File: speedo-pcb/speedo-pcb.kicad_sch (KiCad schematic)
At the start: 54 parts, among them J1 Debug, J2 Mode, J3 Speedo, J4 Power, J5 VBAT, J6 BOOT, J7 Breakout, M1 X27_128, U1 XC6206P332MR, U3 OLED_128x32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

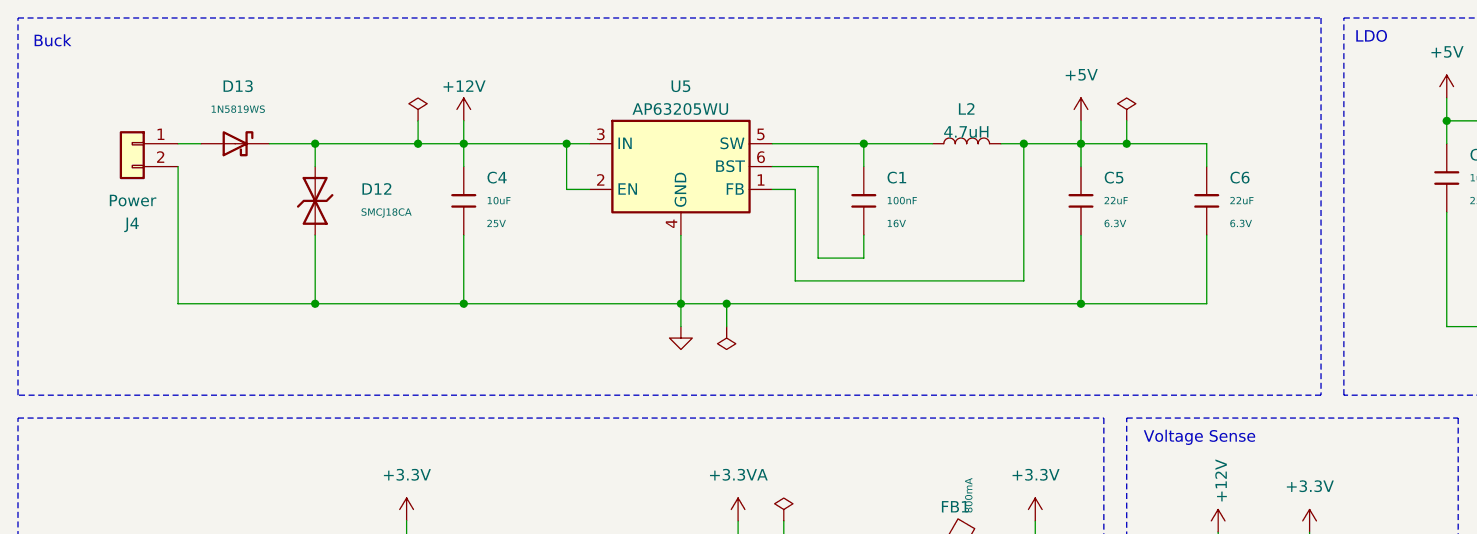
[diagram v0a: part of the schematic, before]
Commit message: buck converter and tvs
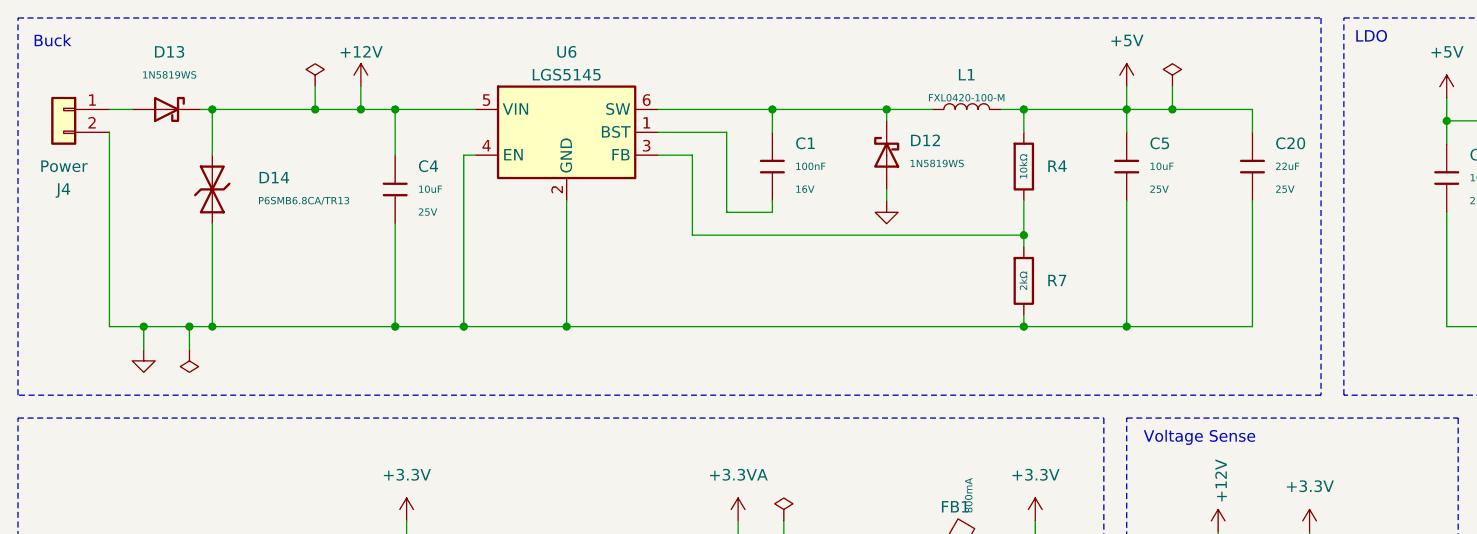
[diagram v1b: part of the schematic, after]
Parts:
- removed C5, C6: 22uF, PCM_JLCPCB:C_0603, symbol PCM_JLCPCB-Capacitors:0603,22uF
- removed D12: SMCJ18CA, PCM_JLCPCB:D_SMC, symbol PCM_JLCPCB-Diodes:TVS-Bi,SMCJ18CA
- removed L2: 4.7uH, Inductor_SMD:L_Chilisin_BMRA00050520, symbol Device:L
- removed U5: AP63205WU, Package_TO_SOT_SMD:TSOT-23-6, symbol Regulator_Switching:AP63205WU
- added C20: 22uF, PCM_JLCPCB:C_0805, symbol PCM_JLCPCB-Capacitors:0805,22uF
- added C5: 10uF, PCM_JLCPCB:C_0805, symbol PCM_JLCPCB-Capacitors:0805,10uF
- added D12: 1N5819WS, PCM_JLCPCB:D_SOD-323, symbol PCM_JLCPCB-Diodes:Schottky,1N5819WS
- added D14: P6SMB6.8CA/TR13, PCM_JLCPCB:D_SMB, symbol PCM_JLCPCB-Diodes:TVS-Bi,P6SMB6.8CA/TR13
- added L1: FXL0420-100-M, Inductor_SMD:L_Sunlord_MWSA0402S, symbol Device:L
- added R4: 10kΩ, PCM_JLCPCB:R_0402, symbol PCM_JLCPCB-Resistors:0402,10kΩ
- added R7: 2kΩ, PCM_JLCPCB:R_0402, symbol PCM_JLCPCB-Resistors:0402,2kΩ
- added U6: LGS5145, Package_TO_SOT_SMD:SOT-23-6, symbol Regulator_Switching:LGS5145
- C1: Stock 28090188 -> 26683372
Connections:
- net +12V: now also D14.2, U6.5 (VIN)
- net +5V: now also C20.1, C5.1, L1.2, R4.1
- net GND: now also C20.2, C5.2, D12.2, D14.1, R7.2, U6.2 (GND), U6.4 (EN)
- net at C1.1: now also U6.1 (BST)
- net at C1.2: now also D12.1, L1.1, U6.6 (SW)
- new net: R4.2, R7.1, U6.3 (FB)
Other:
- moved on the sheet: C4, D13, J4

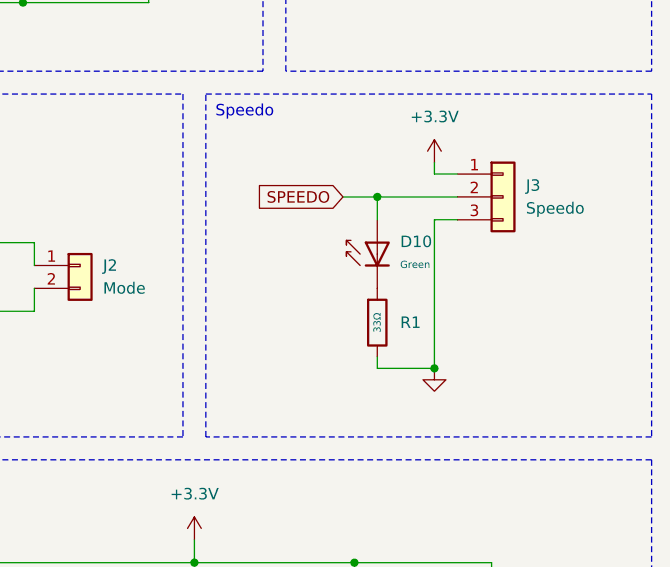
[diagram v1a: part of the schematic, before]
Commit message: buck converter fills
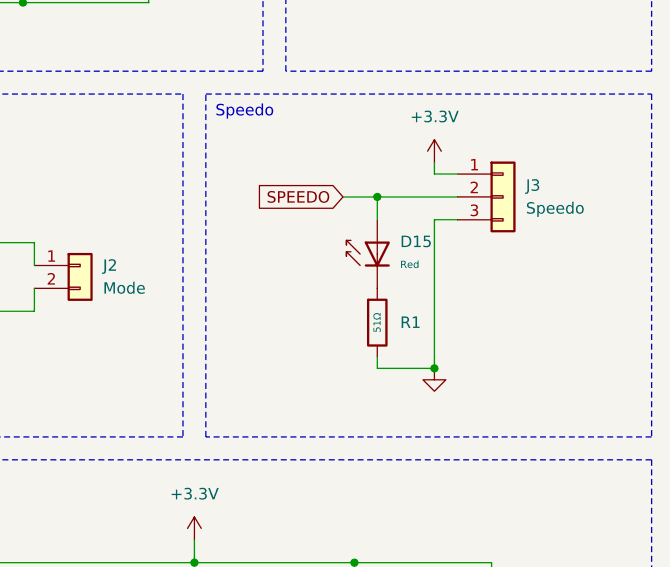
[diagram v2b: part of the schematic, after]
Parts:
- removed D10: Green, PCM_JLCPCB:D_0603, symbol PCM_JLCPCB-Diodes:LED,0603,Green
- removed R1: 33Ω, PCM_JLCPCB:R_0402, symbol PCM_JLCPCB-Resistors:0402,33Ω
- added D15: Red, PCM_JLCPCB:D_0603, symbol PCM_JLCPCB-Diodes:LED,0603,Red
- added R1: 51Ω, PCM_JLCPCB:R_0402, symbol PCM_JLCPCB-Resistors:0402,51Ω
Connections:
- net GND: now also R1.2
- net SPEEDO: now also D15.2
- new net: D15.1, R1.1
